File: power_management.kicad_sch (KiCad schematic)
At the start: 36 parts, among them U1 TPS65185RGZR

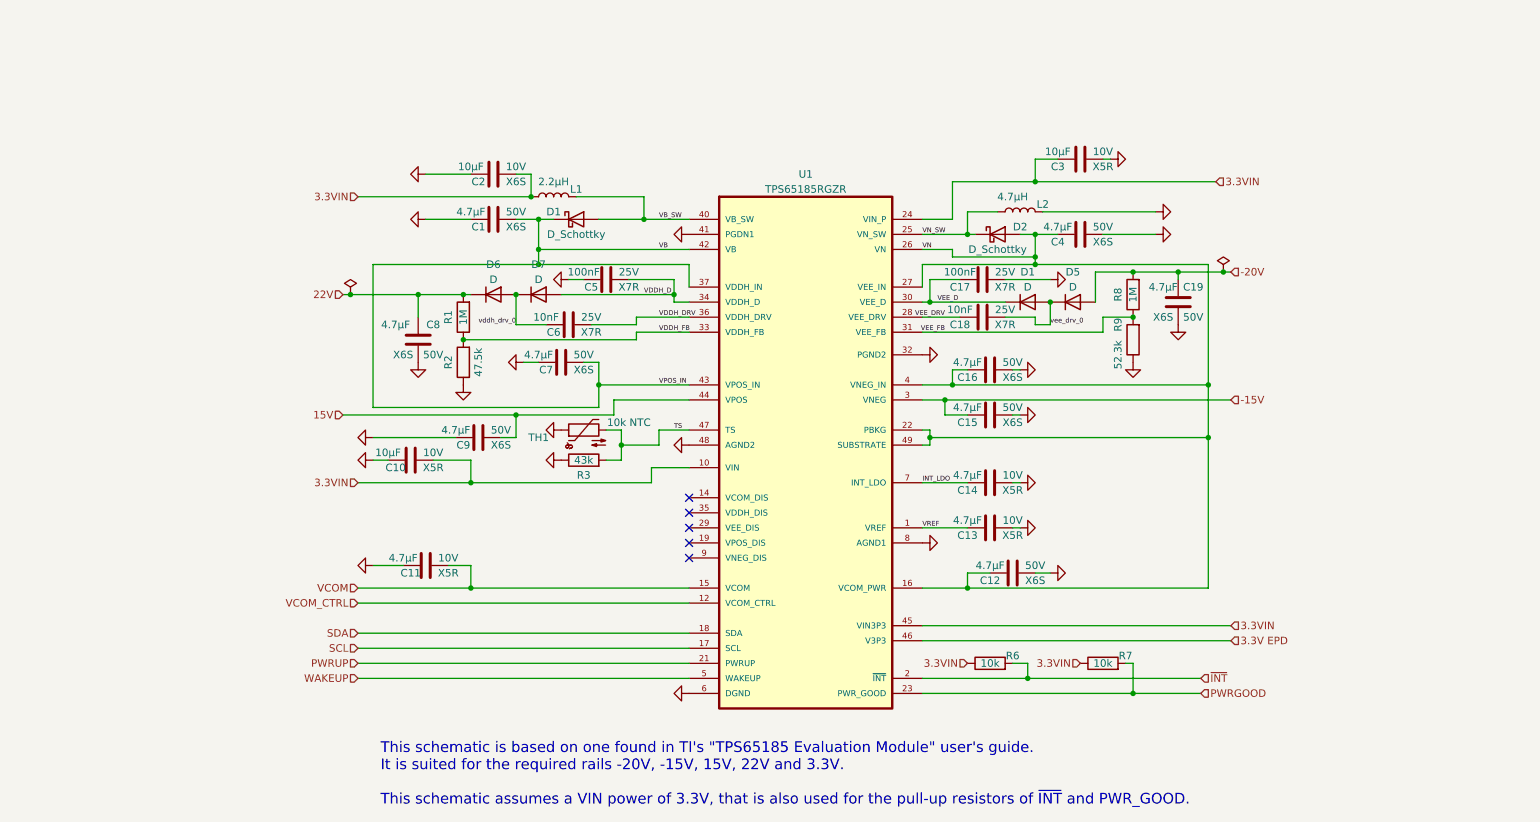
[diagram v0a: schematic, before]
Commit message: Add titles to schematics
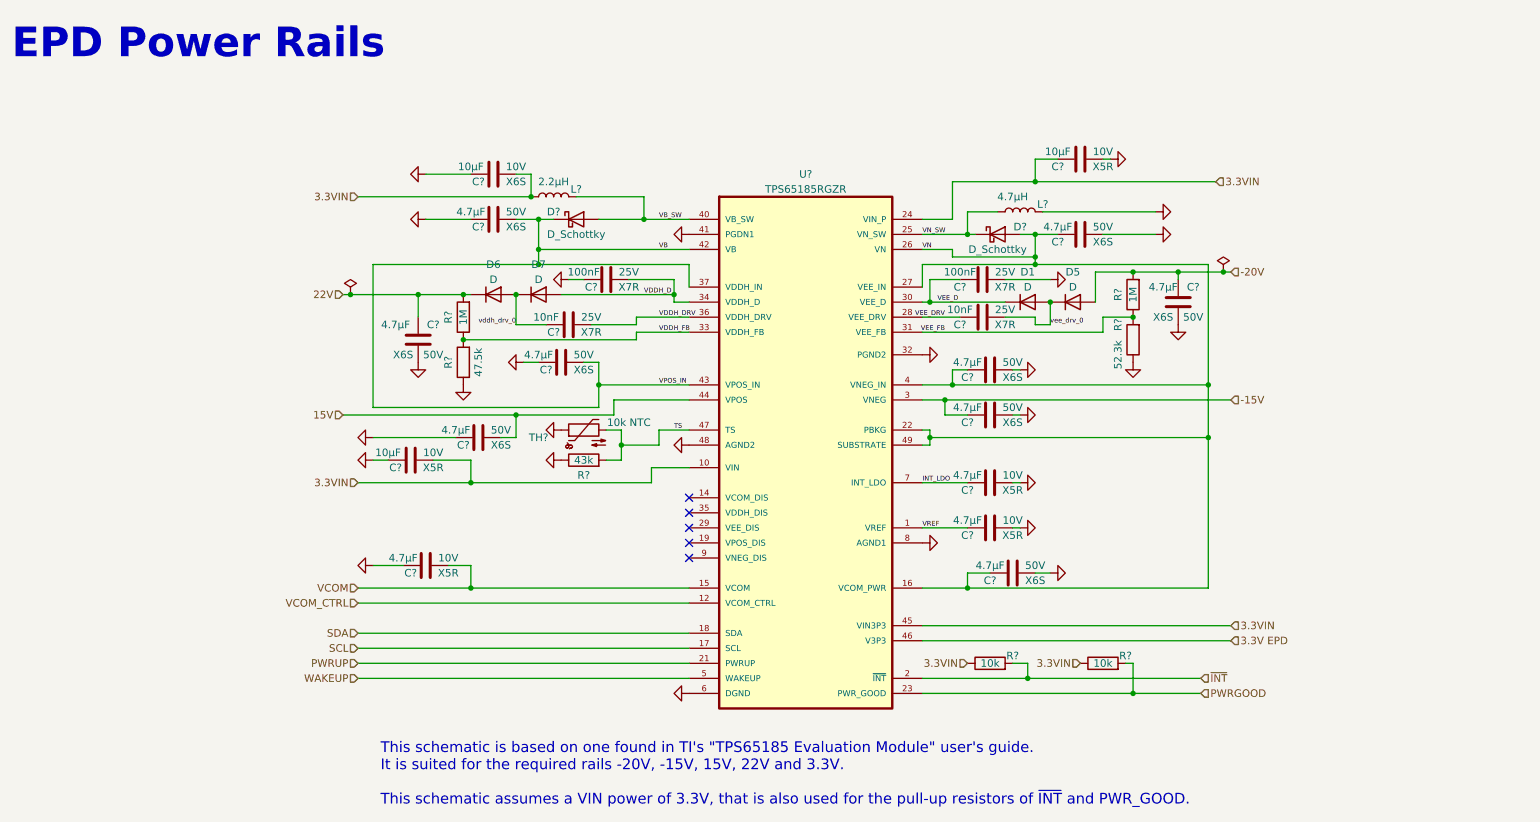
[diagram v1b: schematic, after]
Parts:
- renumbered C14 to C?, C2 to C?, C3 to C?, C1 to C?, C4 to C?, C13 to C?, C9 to C?, C7 to C?, C15 to C?, C11 to C?, C10 to C?, C16 to C?, C12 to C?, C5 to C?, C6 to C?, C17 to C?, C8 to C?, C19 to C?, C18 to C?, D2 to D?, D1 to D?, L2 to L?, L1 to L?, R2 to R?, R1 to R?, R9 to R?, R7 to R?, R8 to R?, R6 to R?, R3 to R?, TH1 to TH?, U1 to U?
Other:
- note added: "EPD Power Rails"
